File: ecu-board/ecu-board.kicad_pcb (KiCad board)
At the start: 2 copper layers, 180 x 130 mm, 61 parts, among them J1 MicroSquirt_connector, J10 Injector connector, J11 Cockpit connector, J12 EGO connector, J13 Chrankshaft Hall connector, J14 Camshaft Hall connector, J15 Ignition 1 connector, J16 Ignition 2 connector, J17 Camera connector, J18 Wheel Hall connector, J19 Speed sensor connector, J2 Battery power conenctor, J20 CAN connector, J3 MS_breakout_conn, J4 Motor connector, J5 Serial DB9 connector, J6 Controller connector, J7 Backlight connector, J8 IAT connector, J9 CLT connector, K1 Main power relay, K2 Start motor relay, U1 MAP Sensor

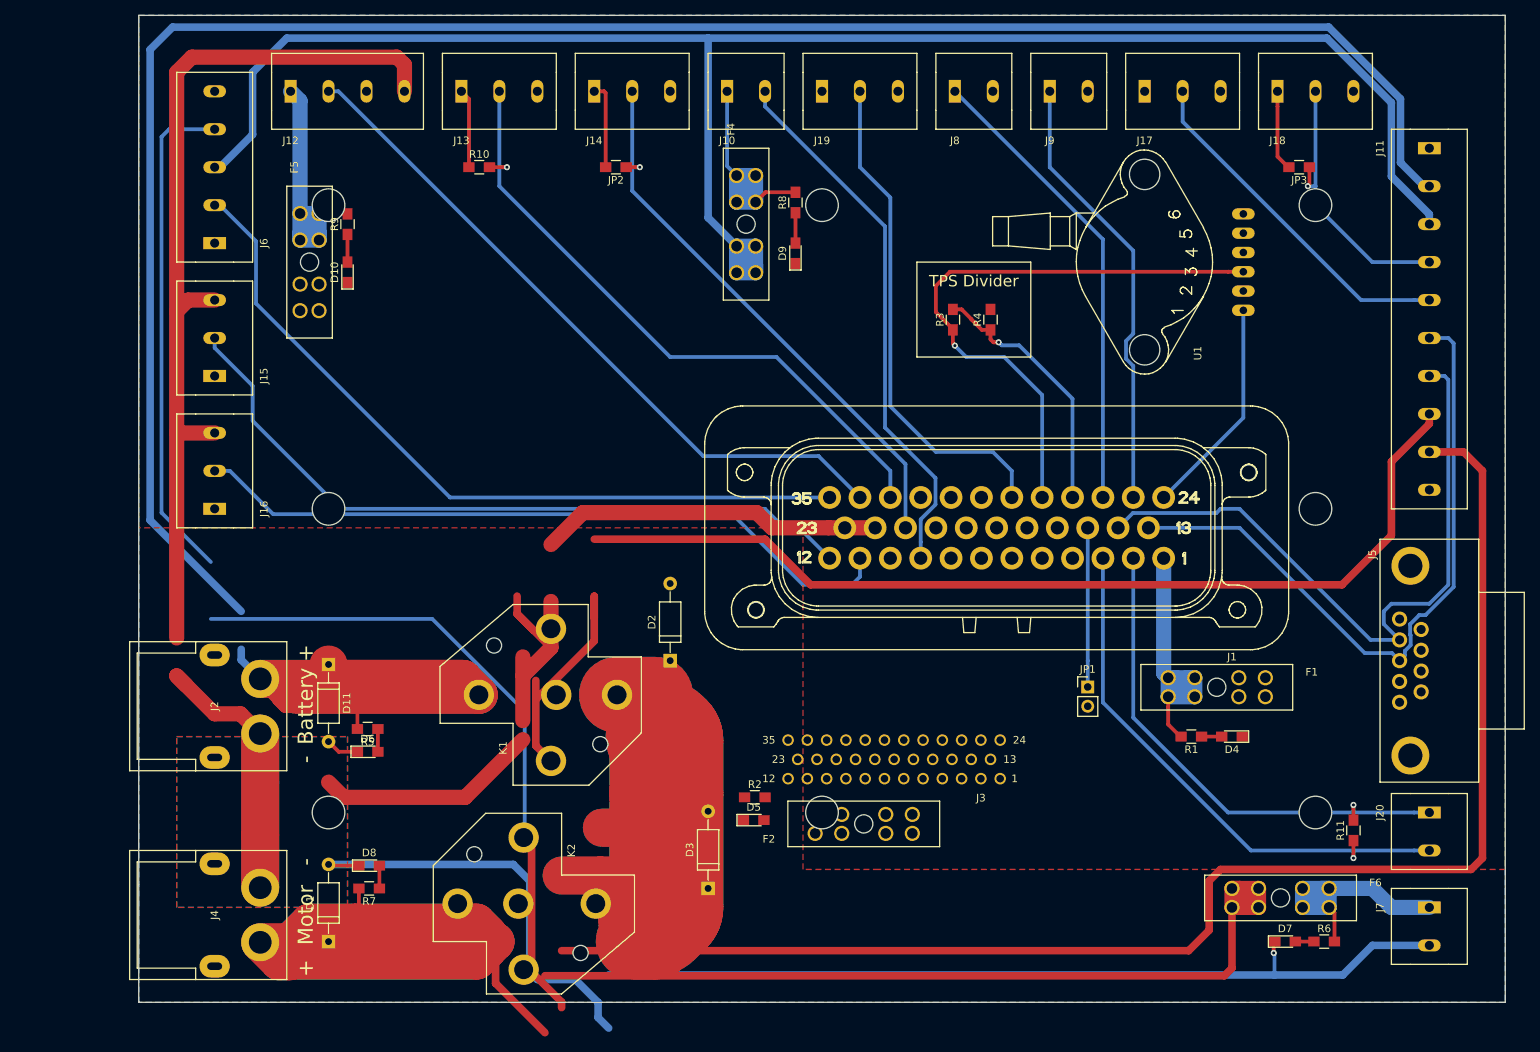
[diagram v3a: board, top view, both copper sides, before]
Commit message: Adjust dimension drawing.
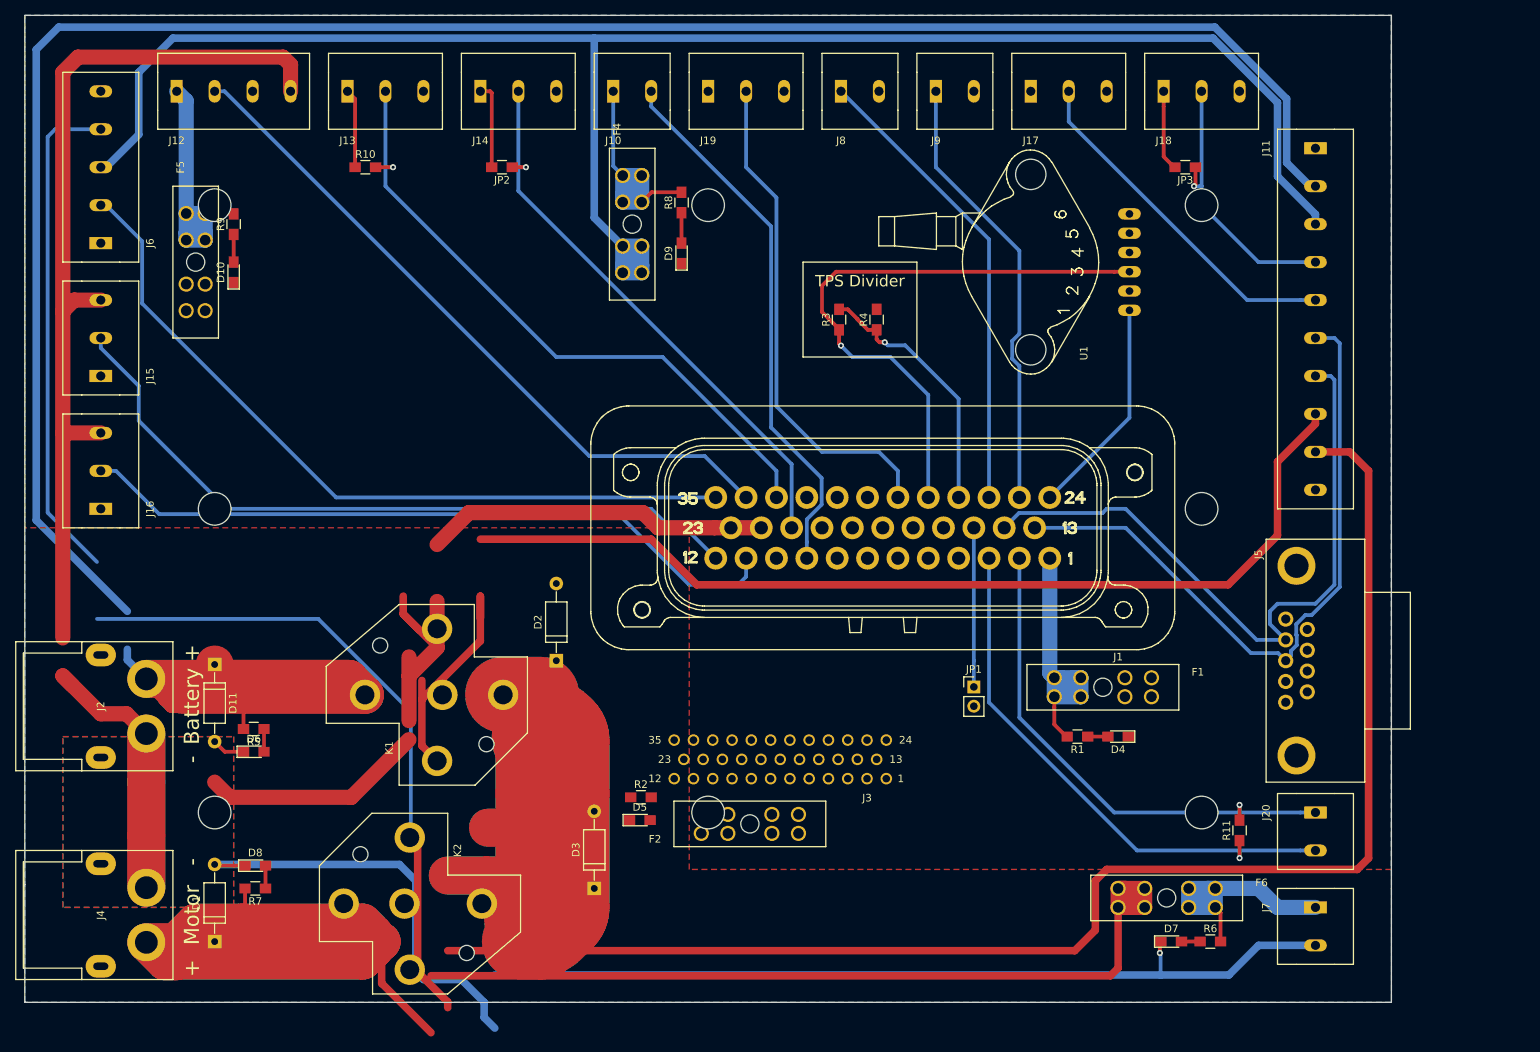
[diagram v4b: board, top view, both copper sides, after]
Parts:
- removed the REF** at (75.0, 100.0)
- removed the REF** at (75.0, 140.0)
- removed the REF** at (140.0, 140.0)
- removed the REF** at (205.0, 140.0)
- removed the REF** at (205.0, 100.0)
- removed the REF** at (205.0, 60.0)
- removed the REF** at (140.0, 60.0)
- removed the REF** at (75.0, 60.0)
- added REF**: MountingHole_4.3mm_M4_DIN965_Pad_Isolated, ecu-board-footprints:MountingHole_4.3mm_M4_DIN965_Pad_Isolated, F.Cu at (60.0, 100.0)
- added REF**: MountingHole_4.3mm_M4_DIN965_Pad_Isolated, ecu-board-footprints:MountingHole_4.3mm_M4_DIN965_Pad_Isolated, F.Cu at (60.0, 140.0)
- added REF**: MountingHole_4.3mm_M4_DIN965_Pad_Isolated, ecu-board-footprints:MountingHole_4.3mm_M4_DIN965_Pad_Isolated, F.Cu at (125.0, 140.0)
- added REF**: MountingHole_4.3mm_M4_DIN965_Pad_Isolated, ecu-board-footprints:MountingHole_4.3mm_M4_DIN965_Pad_Isolated, F.Cu at (190.0, 140.0)
- added REF**: MountingHole_4.3mm_M4_DIN965_Pad_Isolated, ecu-board-footprints:MountingHole_4.3mm_M4_DIN965_Pad_Isolated, F.Cu at (190.0, 100.0)
- added REF**: MountingHole_4.3mm_M4_DIN965_Pad_Isolated, ecu-board-footprints:MountingHole_4.3mm_M4_DIN965_Pad_Isolated, F.Cu at (190.0, 60.0)
- added REF**: MountingHole_4.3mm_M4_DIN965_Pad_Isolated, ecu-board-footprints:MountingHole_4.3mm_M4_DIN965_Pad_Isolated, F.Cu at (125.0, 60.0)
- added REF**: MountingHole_4.3mm_M4_DIN965_Pad_Isolated, ecu-board-footprints:MountingHole_4.3mm_M4_DIN965_Pad_Isolated, F.Cu at (60.0, 60.0)
- moved D1 15.0 mm to (60.0, 157.0)
- moved D10 15.0 mm to (62.5, 68.8)
- moved D11 15.0 mm to (60.0, 120.5)
- moved D2 15.0 mm to (105.0, 120.0)
- moved D3 15.0 mm to (110.0, 150.0)
- moved D4 15.0 mm to (179.0, 130.0)
- moved D5 15.0 mm to (116.0, 141.0)
- moved D6 15.0 mm to (65.2, 132.0)
- moved D7 15.0 mm to (186.0, 157.0)
- moved D8 15.0 mm to (65.3, 147.0)
- moved D9 15.0 mm to (121.5, 66.3)
- moved F1 15.0 mm to (177.0, 123.5)
- moved F2 15.0 mm to (130.5, 141.5)
- moved F4 15.0 mm to (115.0, 62.5)
- moved F5 15.0 mm to (57.5, 67.5)
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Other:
- board text added: "Note: M4 mounting holes. Isolated."

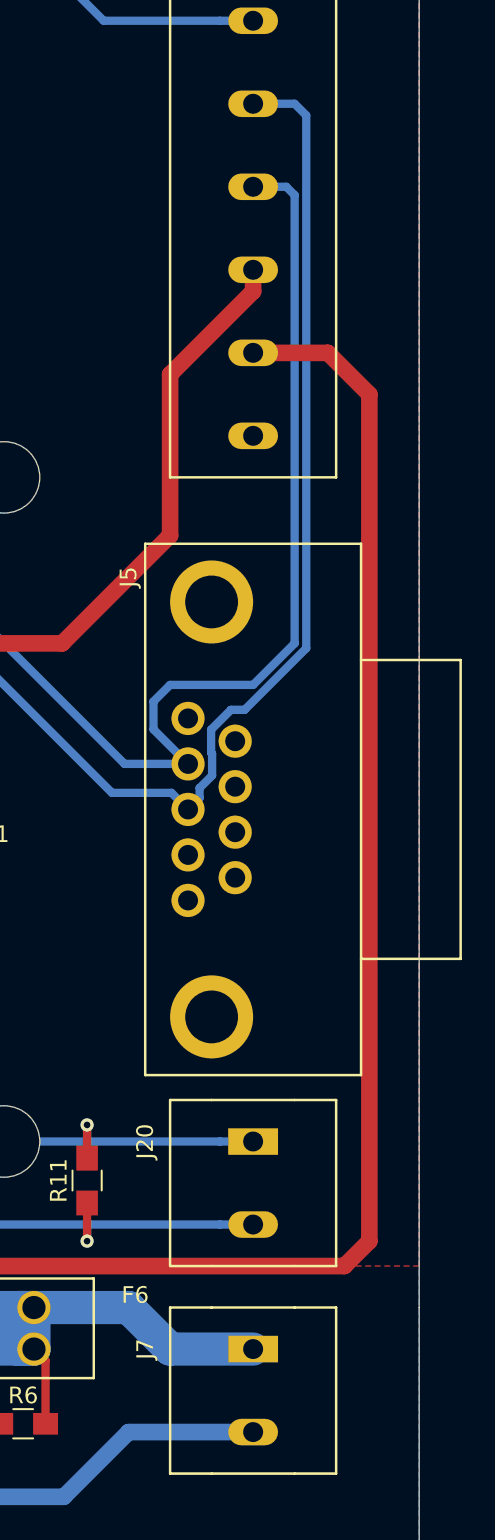
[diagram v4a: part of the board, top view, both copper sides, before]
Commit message: Change cockpit ground from SGND to PWRGND.
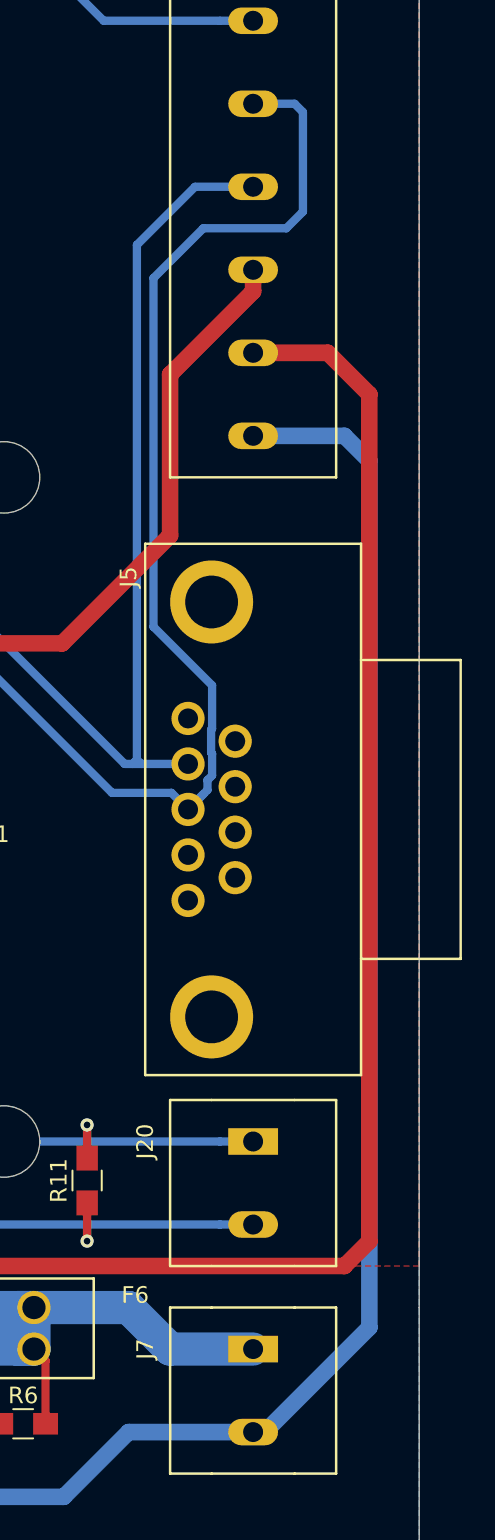
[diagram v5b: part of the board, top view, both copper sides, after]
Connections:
- J11 pad 10: GNDS -> GNDPWR
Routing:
- net GNDPWR: track 459.3 -> 528.8 mm
- net /serial_RX: track 89.1 -> 95.6 mm
- net /serial_TX: track 89.5 -> 85.4 mm

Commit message: Add redundant 12V and PWRGND connectors. Closes #52. Also add PWRGND copper pour.
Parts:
- added J21: 12V connector, ecu-board-footprints:Terminal_Block_4x5.00mm, F.Cu at (140.0, 155.0)
- added J22: PWRGND connector, ecu-board-footprints:Terminal_Block_4x5.00mm, F.Cu at (162.5, 155.0)
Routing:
- net GNDPWR: track 528.8 -> 533.8 mm
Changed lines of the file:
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@@
     (thickness 1.6)
     (drawings 27)
-    (tracks 433)
+    (tracks 434)
     (zones 0)
-    (modules 61)
+    (modules 63)
     (nets 63)
   )
@@
     (add_net GNDPWR)
   )
+  (module ecu-board-footprints:Terminal_Block_4x5.00mm (layer F.Cu)
+    (at 162.5 155 180)
+    (fp_text reference J22 (at 0 6.5) (layer F.SilkS)
+      (effects (font (size 1 1) (thickness 0.15)))
+    )
+    (fp_text value "PWRGND connector" (at 7.5 -6.5) (layer F.Fab)
+      (effects (font (size 1 1) (thickness 0.15)))
+    )
+    (fp_line (start -2.5 5) (end 17.5 5) (layer F.SilkS) (width 0.15))
+    (fp_line (start -2.5 2.5) (end -2.5 5) (layer F.SilkS) (width 0.15))
+    (fp_line (start -2.5 -2.5) (end -2.5 2.5) (layer F.SilkS) (width 0.15))
+    (fp_line (start -2.5 -5) (end -2.5 -2.5) (layer F.SilkS) (width 0.15))
+    (fp_line (start 17.5 -5) (end -2.5 -5) (layer F.SilkS) (width 0.15))
+    (fp_line (start 17.5 5) (end 17.5 -5) (layer F.SilkS) (width 0.15))
+    (fp_line (start -2.5 -2.5) (end -2.5 2.5) (layer F.SilkS) (width 0.15))
+    (pad 4 thru_hole oval (at 15 0 180) (size 1.6 3) (drill 1.2) (layers *.Cu *.Mask)
+      (net 1 GNDPWR))
+    (pad 3 thru_hole oval (at 10 0 180) (size 1.6 3) (drill 1.2) (layers *.Cu *.Mask)
+      (net 1 GNDPWR))
+    (pad 2 thru_hole oval (at 5 0 180) (size 1.6 3) (drill 1.2) (layers *.Cu *.Mask)
+      (net 1 GNDPWR))
+    (pad 1 thru_hole rect (at 0 0 180) (size 1.6 3) (drill 1.2) (layers *.Cu *.Mask)
+      (net 1 GNDPWR))
+  )
+  (module ecu-board-footprints:Terminal_Block_4x5.00mm (layer F.Cu)
+    (at 140 155 180)
+    (fp_text reference J21 (at 0 6.5) (layer F.SilkS)
+      (effects (font (size 1 1) (thickness 0.15)))
+    )
+    (fp_text value "12V connector" (at 7.5 -6.5) (layer F.Fab)
+      (effects (font (size 1 1) (thickness 0.15)))
+    )
+    (fp_line (start -2.5 5) (end 17.5 5) (layer F.SilkS) (width 0.15))
+    (fp_line (start -2.5 2.5) (end -2.5 5) (layer F.SilkS) (width 0.15))
+    (fp_line (start -2.5 -2.5) (end -2.5 2.5) (layer F.SilkS) (width 0.15))
+    (fp_line (start -2.5 -5) (end -2.5 -2.5) (layer F.SilkS) (width 0.15))
+    (fp_line (start 17.5 -5) (end -2.5 -5) (layer F.SilkS) (width 0.15))
+    (fp_line (start 17.5 5) (end 17.5 -5) (layer F.SilkS) (width 0.15))
+    (fp_line (start -2.5 -2.5) (end -2.5 2.5) (layer F.SilkS) (width 0.15))
+    (pad 4 thru_hole oval (at 15 0 180) (size 1.6 3) (drill 1.2) (layers *.Cu *.Mask)
+      (net 6 +12V))
+    (pad 3 thru_hole oval (at 10 0 180) (size 1.6 3) (drill 1.2) (layers *.Cu *.Mask)
+      (net 6 +12V))
+    (pad 2 thru_hole oval (at 5 0 180) (size 1.6 3) (drill 1.2) (layers *.Cu *.Mask)
+      (net 6 +12V))
+    (pad 1 thru_hole rect (at 0 0 180) (size 1.6 3) (drill 1.2) (layers *.Cu *.Mask)
+      (net 6 +12V))
+  )
   (module ecu-board-footprints:TE_5747844-4 (layer F.Cu)
     (at 202.5 120 270)
@@
   (segment (start 210.5 97.5) (end 205 97.5) (width 1) (layer B.Cu) (net 1))
   (segment (start 212 99) (end 210.5 97.5) (width 1) (layer B.Cu) (net 1))
+  (segment (start 40 117) (end 40 122) (width 2) (layer F.Cu) (net 1))
   (segment (start 51 157.1) (end 53.499999 159.599999) (width 5) (layer B.Cu) (net 2) (status 10))
   (segment (start 53.499999 159.599999) (end 54.900001 159.599999) (width 5) (layer B.Cu) (net 2))
@@
     (polygon
       (pts
-        (xy 35 35) (xy 215 35) (xy 215 147.5) (xy 132.5 147.5) (xy 122.5 147.5)
+        (xy 35 35) (xy 215 35) (xy 215 135) (xy 132.5 135) (xy 122.5 135)
         (xy 122.5 102.5) (xy 35 102.5)
       )
@@
   )
   (zone (net 1) (net_name GNDPWR) (layer F.Cu) (hatch edge 0.508)
+    (priority 3)
     (connect_pads (clearance 0.508))
     (min_thickness 0.254)
@@
   )
   (zone (net 1) (net_name GNDPWR) (layer B.Cu) (hatch edge 0.508)
+    (priority 3)
     (connect_pads (clearance 0.508))
     (min_thickness 0.254)
@@
       )
     )
+  )
+  (zone (net 1) (net_name GNDPWR) (layer F.Cu) (hatch edge 0.508)
+    (priority 3)
+    (connect_pads (clearance 0.508))
+    (min_thickness 0.254)
+    (fill yes (arc_segments 32) (thermal_gap 0.508) (thermal_bridge_width 0.508))
+    (polygon
+      (pts
+        (xy 35 107.5) (xy 117.5 107.5) (xy 117.5 140) (xy 215 140) (xy 215 165)
+        (xy 35 165)
+      )
+    )
